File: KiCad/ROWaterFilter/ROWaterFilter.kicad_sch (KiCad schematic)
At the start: 32 parts, among them J1 Power board, J10 Low P Sensor, J2 Power board, J3 High P Sensor, J4 High P Sensor, J5 Actuators terminals, J6 Analog, J7 Digital, J8 PSU Terminals, J9 Low P Sensor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

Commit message: release
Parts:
- removed J3: High P Sensor, symbol Connector:Conn_01x02_Pin
- removed J4: High P Sensor, symbol Connector:Conn_01x02_Socket
- removed J9: Low P Sensor, symbol Connector:Conn_01x02_Socket
- removed K2, K3: 12V, Relay_THT:Relay_SPDT_Omron-G5LE-1, symbol Relay:G5LE-1
- removed Q2: BJT, Package_TO_SOT_THT:TO-92_Inline, symbol Transistor_BJT:MMBT2222A
- removed R5: 10k, symbol Device:R
- added D4: 1N4007, Diode_THT:D_DO-41_SOD81_P10.16mm_Horizontal, symbol Diode:1N4007
- added D5: КД243Е, symbol Simulation_SPICE:D
- added J11: High P Sensor, symbol Connector:Conn_01x01_Pin
- added J3: High P Sensor, symbol Connector:Conn_01x03_Socket
- added J4: Low P Sensor, symbol Connector:Conn_01x04_Socket
- added K2: Intake shutoff valve, symbol Relay:COTO_3660_Split
- added Q2: P0903BDG, symbol Simulation_SPICE:NMOS
- added R6: 17k, symbol Device:R
- added U1: PC123, symbol Isolator:Optocoupler_DC_PhotoNPN_AKEC
- J5: Name (none) -> OUT
- J8: Name (none) -> IN
- K1: value ${SIM.PARAMS} -> Automatic flushing valve; footprint Relay_THT:Relay_3PST_COTO_3660 -> (none)
- M1: value ${SIM.PARAMS} -> Pump
- Q1: value NMOS -> P0903BDG
- R1: value 5k -> 1k
- SW2: value Ignore Low P -> Maintenance mode switch
- V1: value 1 -> 24V 2A
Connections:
- net A2: now also J4.1 (Pin_1)
- net A3: now also U1.4
- net at J1.1 (Pin_1), J6.GND (Pin_11): now also J4.4 (Pin_4), U1.3
- net at C3.2, D1.2 (A), J5.2 (Pin_2): now also Q2.1 (D); no longer Q1.1 (D)
- net at J5.3 (Pin_3), K1.A2, M1.2 (-): now also D5.2 (A), K2.A2
- net at J5.4 (Pin_4): now also SW1.1 (A)
- net at C1.2, C2.1, J2.1 (Pin_1)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: now also J2.4 (Pin_4)
- net at R1.1: now also Q1.2 (G), R4.1, Q2.2 (G)
- net at J8.1 (Pin_1), V1.1: no longer SW1.1 (A)
- net at J1.4 (Pin_4): now also D4.2 (A), U1.2
- net at K1.A1, M1.1 (+): now also SW1.2 (B), D5.1 (K), J11.1 (Pin_1), K2.A1
- new net: D4.1 (K), J3.1_Y (Pin_1), R6.1
- new net: R6.2, U1.1
- new net: Q1.1 (D), Q2.3 (S)
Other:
- moved on the sheet: C1, C2, C3, D1, J1, J10, M1, Q1, R4, SW1, SW3

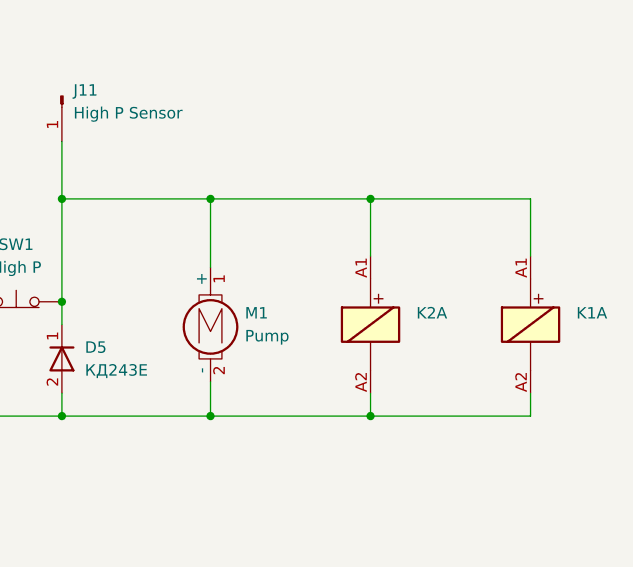
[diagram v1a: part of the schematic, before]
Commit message: add: manual, description to readme; comments in code
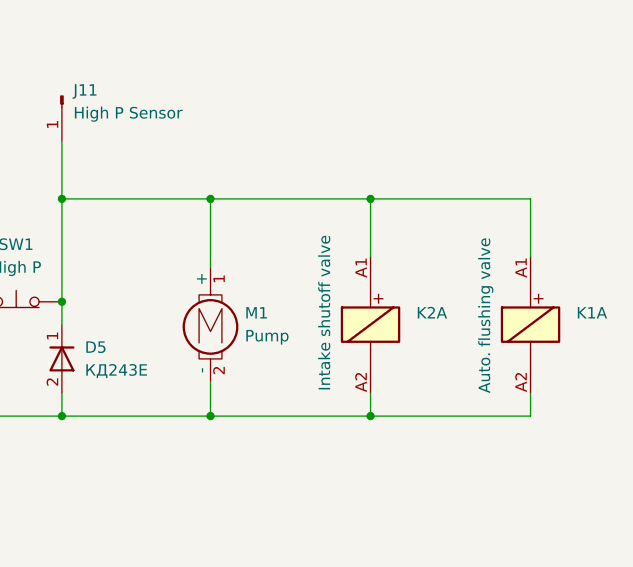
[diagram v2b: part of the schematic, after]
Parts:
- K1: value Automatic flushing valve -> Auto. flushing valve
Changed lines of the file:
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@@
 		(on_board no)
 		(dnp no)
-		(fields_autoplaced yes)
 		(property "Reference" "K1"
 			(at 274.32 129.5399 0)
@@
 			)
 		)
-		(property "Value" "Automatic flushing valve"
-			(at 274.32 132.0799 0)
-			(effects
-				(font
-					(size 1.27 1.27)
-				)
-				(justify left)
-				(hide yes)
+		(property "Value" "Auto. flushing valve"
+			(at 264.16 138.43 90)
+			(effects
+				(font
+					(size 1.27 1.27)
+				)
+				(justify left)
 			)
 		)
@@
 		(on_board no)
 		(dnp no)
-		(fields_autoplaced yes)
 		(property "Reference" "K2"
 			(at 256.54 129.5399 0)
@@
 		)
 		(property "Value" "Intake shutoff valve"
-			(at 256.54 132.0799 0)
-			(effects
-				(font
-					(size 1.27 1.27)
-				)
-				(justify left)
-				(hide yes)
-			)
-		)
+			(at 246.38 138.176 90)
+			(effects
+				(font
+					(size 1.27 1.27)
+				)
+				(justify left)
+			)
+		)

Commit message: docs, refactor, feat: readme update, refactor timers in lib, add time calibration function
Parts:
- SW2: footprint (none) -> Button_Switch_THT:SW_Slide_SPDT_Angled_CK_OS102011MA1Q
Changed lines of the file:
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@@
 			)
 		)
-		(property "Footprint" ""
+		(property "Footprint" "Button_Switch_THT:SW_Slide_SPDT_Angled_CK_OS102011MA1Q"
 			(at 41.91 59.69 0)
 			(effects
